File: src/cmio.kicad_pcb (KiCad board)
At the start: 2 copper layers, 72.4 x 36.8 mm, 37 parts, among them J15 CONN_01X02, J2 BANK0, J4 DSI0, J5 CM3Lite, J6 DSI1, J8 BANK1, J9 Micro_SD_Card_TFP09_2_12B, U1 ISL91107IR, U2 LD3985M18R, U3 LD3985M28R

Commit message: Some changes to old design
Signed-off-by: Mahyar Koshkouei <mk@deltabeard.com>
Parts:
- removed 1V8: TEST_1V8, Measurement_Points:Measurement_Point_Round-SMD-Pad_Small
- removed 2V8: TEST_2V8, Measurement_Points:Measurement_Point_Round-SMD-Pad_Small
- removed 3V3: TEST_3V3, Measurement_Points:Measurement_Point_Round-SMD-Pad_Small
- removed 5V: TEST_5V, Measurement_Points:Measurement_Point_Round-SMD-Pad_Small
- removed GND: TEST_GND, Measurement_Points:Measurement_Point_Round-SMD-Pad_Small
- removed J15: CONN_01X02, Pin_Headers:Pin_Header_Straight_2x01_Pitch2.54mm_SMD
- removed J2: BANK0, Pin_Headers:Pin_Header_Straight_2x20_Pitch2.54mm_SMD
- removed J6: DSI1, Pin_Headers:Pin_Header_Straight_2x05_Pitch2.54mm_SMD
- removed JP4: 3.3 OUT, Pin_Headers:Pin_Header_Straight_2x01_Pitch2.54mm_SMD
- removed JP6: PWRUSB, Pin_Headers:Pin_Header_Straight_2x01_Pitch2.54mm_SMD
- removed JP7: Disable SD Card, Pin_Headers:Pin_Header_Straight_2x01_Pitch2.54mm_SMD
- removed POWER: USB_POWER, foot:Micro_USB_B_10104110_no_holes
- removed RESET: Reset, Buttons_Switches_SMD:SW_SPST_TL3342
- removed TV: TVOUT, foot:RCA_PHONO
- removed USB: USB_OTG, foot:Micro_USB_B_10104110_no_holes
- added C11: 4.7uF, Capacitors_SMD:C_1206_HandSoldering, F.Cu at (208.2, 67.3)
- added J1: USB_POWER, foot:Micro_USB_B_10104110, F.Cu at (178.4, 61.0)
- added J10: CM3Lite, foot:Socket_SODIMM_DDR1-2_TE_1612618, B.Cu at (190.5, 76.2)
- added J11: TVOUT, foot:RCA_PHONO, F.Cu at (157.5, 83.8)
- added J12: BANK1, Pin_Headers:Pin_Header_Straight_2x10_Pitch2.54mm_SMD, F.Cu at (196.8, 73.7)
- added J13: Micro_SD_Card_TFP09_2_12B, foot:TFP09-2-12B, F.Cu at (213.4, 66.0)
- added J7: TEST_GND, Measurement_Points:Measurement_Point_Round-SMD-Pad_Small, F.Cu at (157.5, 58.4)
- added JP1: 3.3 OUT, Pin_Headers:Pin_Header_Straight_2x01_Pitch2.54mm_SMD, F.Cu at (204.5, 62.9)
- added JP2: PWRUSB, Pin_Headers:Pin_Header_Straight_2x01_Pitch2.54mm_SMD, F.Cu at (177.0, 64.3)
- added SW1: Reset, Buttons_Switches_SMD:SW_SPST_TL3342, F.Cu at (168.9, 82.5)
- C10: value 4.7uF -> 22uF; moved to F.Cu
- C2, C4, C8, R1, R2: moved to B.Cu
- C3: value 22uF -> 10nF
- C5: value 10nF -> 1uF
- C6: value 22uF -> 1uF
- C7: value 1uF -> 22uF
- J4: value DSI0 -> TEST_3V3; footprint Pin_Headers:Pin_Header_Straight_2x03_Pitch2.54mm_SMD -> Measurement_Points:Measurement_Point_Round-SMD-Pad_Small
- J5: value CM3Lite -> TEST_2V8; footprint foot:Socket_SODIMM_DDR1-2_TE_1612618 -> Measurement_Points:Measurement_Point_Round-SMD-Pad_Small; moved to F.Cu
- J8: value BANK1 -> BANK0; footprint Pin_Headers:Pin_Header_Straight_2x10_Pitch2.54mm_SMD -> Pin_Headers:Pin_Header_Straight_2x20_Pitch2.54mm_SMD
- J9: value Micro_SD_Card_TFP09_2_12B -> USB_OTG; footprint foot:TFP09-2-12B -> foot:Micro_USB_B_10104110; moved to F.Cu
- U1: value ISL91107IR -> LD3985M18R; footprint foot:20_TQFP -> TO_SOT_Packages_SMD:SOT-23-5
- U2: value LD3985M18R -> LD3985M28R; moved to B.Cu
- U3: value LD3985M28R -> ISL91107IR; footprint TO_SOT_Packages_SMD:SOT-23-5 -> foot:20_TQFP
- moved C9 107.4 mm to (195.6, 64.8), turned to 90 degrees
- moved L1 101.2 mm to (190.5, 58.4)
- moved C7 94.1 mm to (182.9, 64.8), turned to 270 degrees
- moved U3 86.6 mm to (190.5, 64.1), turned to 270 degrees
- moved C5 82.6 mm to (185.4, 64.8), turned to 270 degrees
- moved C6 82.2 mm to (169.5, 75.6)
- moved U1 82.0 mm to (169.5, 72.4), turned to 180 degrees
- moved C3 80.7 mm to (163.8, 71.1), turned to 180 degrees
- moved C1 78.8 mm to (175.3, 71.1), turned to 0 degrees
- moved C4 78.7 mm to (172.7, 67.3)
- moved U2 74.4 mm to (167.0, 66.7), turned to 270 degrees
- moved J8 74.2 mm to (199.4, 82.5)
- moved R1 69.4 mm to (214.0, 66.7), turned to 90 degrees
- moved J4 69.0 mm to (157.5, 61.0), turned to 0 degrees
- moved C10 68.6 mm to (198.1, 64.8), turned to 90 degrees
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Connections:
- C1 pad 1: +5V -> +3V3
- C10 pad 1: +3V3 -> GND
- C10 pad 2: GND -> Net-(C10-Pad2)
- C2 pad 1: +5V -> +3V3
- C3 pad 1: +5V -> Net-(C3-Pad1)
- C5 pad 1: Net-(C5-Pad1) -> +5V
- C6 pad 1: GND -> +1V8
- C6 pad 2: Net-(C6-Pad2) -> GND
- C7 pad 1: +1V8 -> +5V
- C9 pad 2: Net-(C6-Pad2) -> Net-(C10-Pad2)
- J4 pad 1: /DSI0_0 -> +3V3
- J5 pad 1: GND -> +2V8
- J8 pad 10: /BCM_40 -> /BCM_15
- J8 pad 11: /BCM_32 -> /BCM_17
- J8 pad 12: /BCM_41 -> /BCM_18
- J8 pad 13: /BCM_33 -> /BCM_27
- J8 pad 14: /BCM_42 -> GND
- J8 pad 15: /BCM_34 -> /BCM_22
- J8 pad 16: /BCM_43 -> /BCM_23
- J8 pad 17: /BCM_35 -> +3V3
- J8 pad 18: /BCM_44 -> /BCM_24
- J8 pad 19: /BCM_36 -> /BCM_10
- J8 pad 2: GND -> +5V
- J8 pad 20: /BCM_45 -> GND
- J8 pad 3: /BCM_28 -> /BCM_2
- J8 pad 4: /BCM_37 -> +5V
- J8 pad 5: /BCM_29 -> /BCM_3
- J8 pad 6: /BCM_38 -> GND
- J8 pad 7: /BCM_30 -> /BCM_4
- J8 pad 8: /BCM_39 -> /BCM_14
- J8 pad 9: /BCM_31 -> GND
- J9 pad 1: DAT2 -> Net-(J9-Pad1)
- J9 pad 2: DAT3 -> /D-
- J9 pad 3: CMD -> /D+
- J9 pad 4: +3V3 -> OTDIG
- J9 pad 5: CLK -> GND
- U1 pad 1: Net-(L1-Pad1) -> +3V3
- U1 pad 2: Net-(L1-Pad1) -> GND
- U1 pad 3: GND -> +3V3
- U1 pad 4: GND -> Net-(C3-Pad1)
- U1 pad 5: Net-(L1-Pad2) -> +1V8
- U2 pad 1: +5V -> +3V3
- U2 pad 3: +5V -> +3V3
- U2 pad 5: +1V8 -> +2V8
- U3 pad 1: +5V -> Net-(L1-Pad1)
- U3 pad 2: GND -> Net-(L1-Pad1)
- U3 pad 3: +5V -> GND
- U3 pad 4: Net-(C5-Pad1) -> GND
- U3 pad 5: +2V8 -> Net-(L1-Pad2)
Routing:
- net +3V3: track 208.1 -> 105.8 mm, vias 14 -> 8
- net +5V: track 132.1 -> 31.1 mm, vias 5 -> 2
- net Net-(J5-Pad177): track 39.6 -> 0.00 mm, vias 1 -> 0
- net +2V8: track 58.9 -> 20.1 mm, vias 2 -> 1
- net /DSI0_1: track 29.1 -> 0.00 mm, vias 1 -> 0
- net /DSI0_0: track 27.4 -> 0.00 mm, vias 1 -> 0
- net +1V8: track 49.6 -> 22.2 mm
- net /BCM_44: track 43.5 -> 16.2 mm
- net /DSI0_3: track 26.7 -> 0.00 mm, vias 1 -> 0
- net /DSI1_8: track 24.7 -> 0.00 mm, vias 1 -> 0
- net TVDAC: track 23.8 -> 0.00 mm, vias 3 -> 0
- net /DSI0_2: track 23.4 -> 0.00 mm, vias 1 -> 0
- net /DSI1_6: track 21.8 -> 0.00 mm, vias 1 -> 0
- net /BCM_45: track 36.4 -> 14.9 mm
- net /DSI1_9: track 21.3 -> 0.00 mm, vias 1 -> 0
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- added copper zone on F.Cu, net +3V3
- added copper zone on F.Cu, net Net-(C10-Pad2)
- added copper zone on F.Cu, net Net-(L1-Pad1)
- added copper zone on F.Cu, net Net-(L1-Pad2)
- removed copper zone on F.Cu, net Net-(C6-Pad2)
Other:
- board size 72.4 x 36.8 mm -> 71.1 x 31.7 mm
- net class Default: clearance 0.16 -> 0; trace_width 0.18 -> 0.25
- net class PWR: clearance 0.2 -> 0.25; trace_width 0.25 -> 0.35
- rule trace_clearance: 0.16 -> 0
- rule trace_min: 0.15 -> 0.2
- rule via_min_size: 0.5 -> 0.6
- board text removed: "GPL 3 Mahyar Koshkouei Custom CMIO Board"

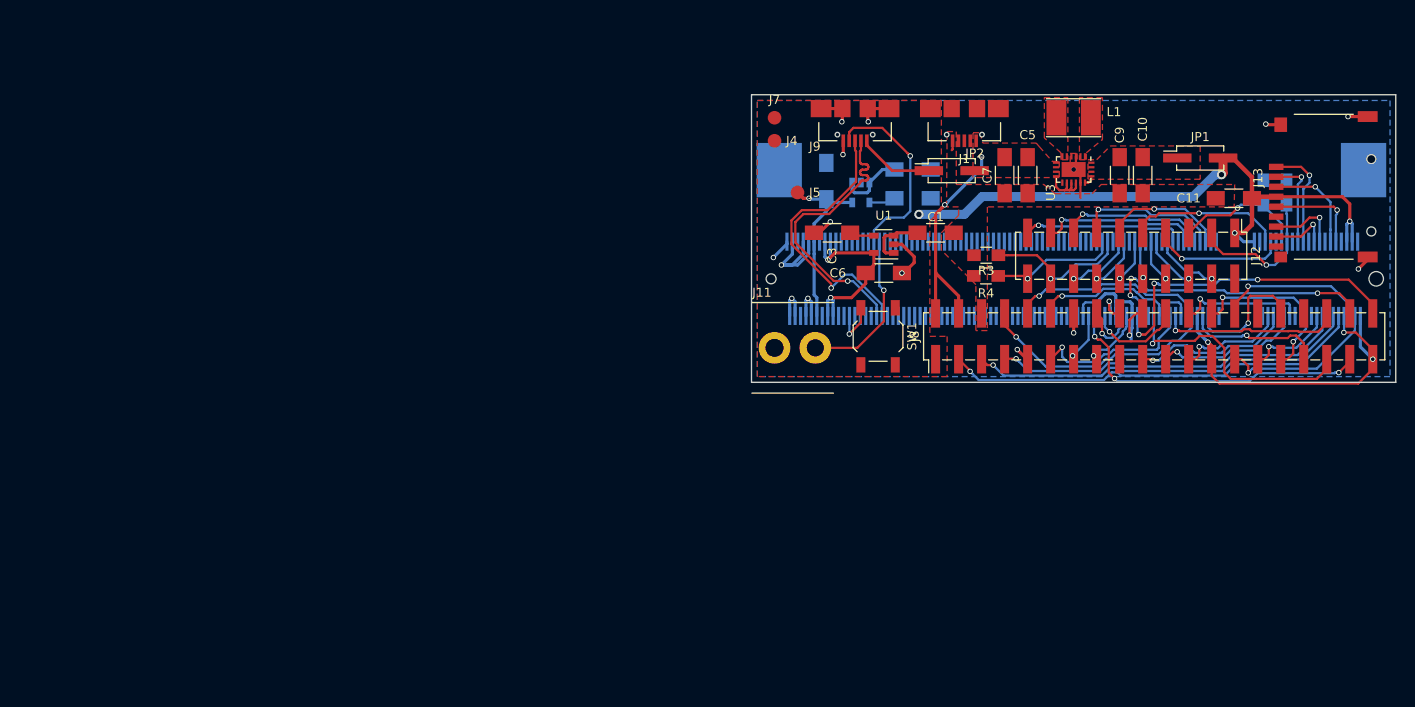
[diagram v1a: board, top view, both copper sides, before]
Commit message: Finish PCB Routing
Signed-off-by: Mahyar Koshkouei <mk@deltabeard.com>
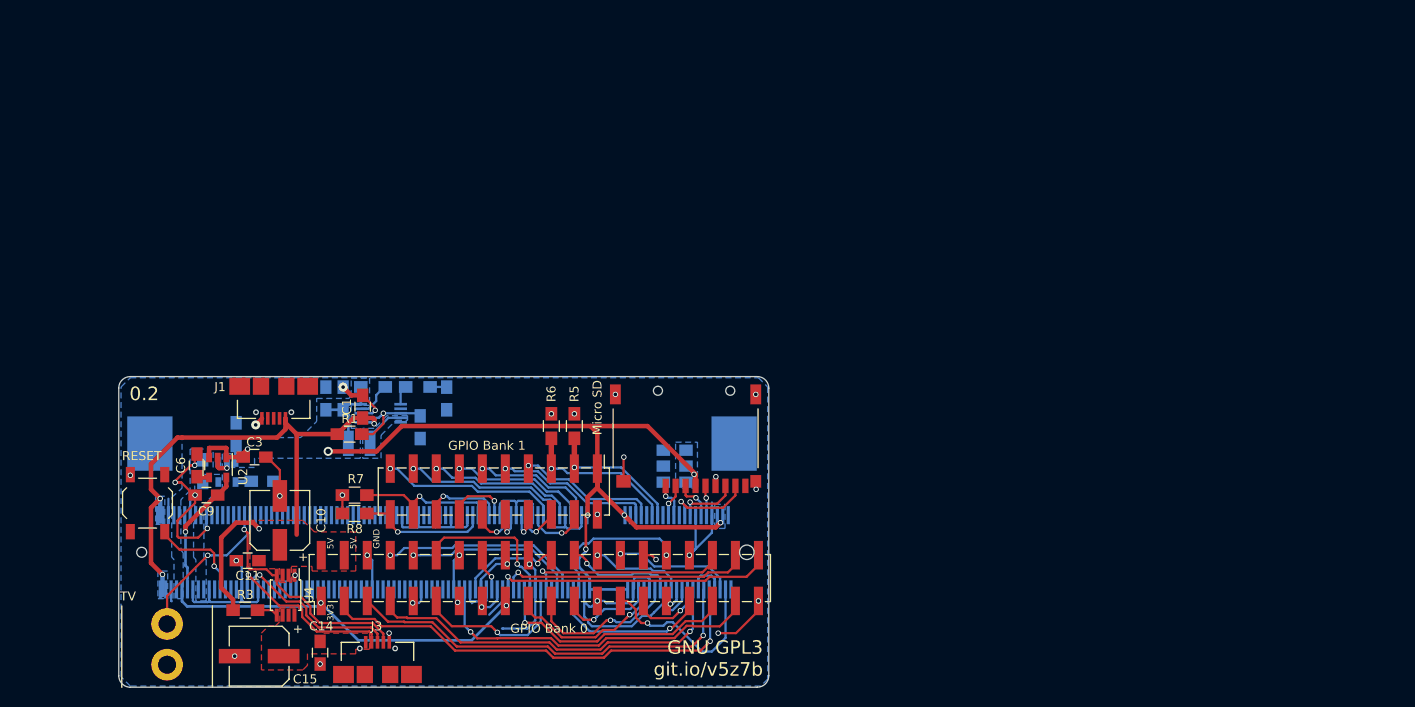
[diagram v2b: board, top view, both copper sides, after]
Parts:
- removed J10: CM3Lite, foot:Socket_SODIMM_DDR1-2_TE_1612618
- removed J11: TVOUT, foot:RCA_PHONO
- removed J12: BANK1, Pin_Headers:Pin_Header_Straight_2x10_Pitch2.54mm_SMD
- removed J13: Micro_SD_Card_TFP09_2_12B, foot:TFP09-2-12B
- removed J8: BANK0, Pin_Headers:Pin_Header_Straight_2x20_Pitch2.54mm_SMD
- removed J9: USB_OTG, foot:Micro_USB_B_10104110
- removed JP1: 3.3 OUT, Pin_Headers:Pin_Header_Straight_2x01_Pitch2.54mm_SMD
- removed JP2: PWRUSB, Pin_Headers:Pin_Header_Straight_2x01_Pitch2.54mm_SMD
- added C12: 10uF, Capacitors_SMD:C_0805_HandSoldering, B.Cu at (109.9, 89.4)
- added C13: 100pF, Capacitors_SMD:C_0805_HandSoldering, B.Cu at (108.0, 89.4)
- added C14: 0.1uF, Capacitors_SMD:C_0805_HandSoldering, F.Cu at (107.3, 117.5)
- added C15: 120uF, Capacitors_SMD:CP_Elec_6.3x5.8, F.Cu at (100.6, 117.9)
- added C16: 100pF, Capacitors_SMD:C_0805_HandSoldering, B.Cu at (146.5, 98.7)
- added C17: 0.1uF, Capacitors_SMD:C_0805_HandSoldering, B.Cu at (146.5, 96.9)
- added C18: 10uF, Capacitors_SMD:C_0805_HandSoldering, B.Cu at (146.5, 95.1)
- added J2: BANK0, Pin_Headers:Pin_Header_Straight_2x20_Pitch2.54mm_SMD, F.Cu at (131.6, 109.2)
- added J3: USB_OTG, foot:Micro_USB_B_10104110, F.Cu at (113.7, 116.3)
- added J6: BANK1, Pin_Headers:Pin_Header_Straight_2x10_Pitch2.54mm_SMD, F.Cu at (126.5, 99.7)
- added R5: 100K, Resistors_SMD:R_0805_HandSoldering, F.Cu at (135.4, 92.5)
- added R6: 100K, Resistors_SMD:R_0805_HandSoldering, F.Cu at (132.8, 92.5)
- added R7: 100K, Resistors_SMD:R_0805_HandSoldering, F.Cu at (111.1, 100.1)
- added R8: 100K, Resistors_SMD:R_0805_HandSoldering, F.Cu at (111.1, 102.1)
- added U4: AP2401, Housings_SSOP:MSOP-8_3x3mm_Pitch0.65mm, F.Cu at (103.5, 111.1)
- C1: value 1uF -> 10uF; footprint Capacitors_SMD:C_1206_HandSoldering -> Capacitors_SMD:C_0805_HandSoldering
- C10: value 22uF -> 120uF; footprint Capacitors_SMD:C_1206_HandSoldering -> Capacitors_SMD:CP_Elec_6.3x5.8
- C11: value 4.7uF -> 0.1uF; footprint Capacitors_SMD:C_1206_HandSoldering -> Capacitors_SMD:C_0805_HandSoldering
- C2, C8: footprint Capacitors_SMD:C_1206_HandSoldering -> Capacitors_SMD:C_0805_HandSoldering
- C3, C4: value 10nF -> 1uF; footprint Capacitors_SMD:C_1206_HandSoldering -> Capacitors_SMD:C_0805_HandSoldering
- C5: value 1uF -> 10nF; footprint Capacitors_SMD:C_1206_HandSoldering -> Capacitors_SMD:C_0805_HandSoldering; moved to B.Cu
- C6: value 1uF -> 10nF; footprint Capacitors_SMD:C_1206_HandSoldering -> Capacitors_SMD:C_0805_HandSoldering
- C7: value 22uF -> 100pF; footprint Capacitors_SMD:C_1206_HandSoldering -> Capacitors_SMD:C_0805_HandSoldering; moved to B.Cu
- C9: value 22uF -> 1uF; footprint Capacitors_SMD:C_1206_HandSoldering -> Capacitors_SMD:C_0805_HandSoldering
- J4: value TEST_3V3 -> CM3Lite; footprint Measurement_Points:Measurement_Point_Round-SMD-Pad_Small -> foot:Socket_SODIMM_DDR1-2_TE_1612618; moved to B.Cu
- J5: value TEST_2V8 -> TVOUT; footprint Measurement_Points:Measurement_Point_Round-SMD-Pad_Small -> foot:RCA_PHONO
- J7: value TEST_GND -> Micro_SD_Card_TFP09_2_12B; footprint Measurement_Points:Measurement_Point_Round-SMD-Pad_Small -> foot:TFP09-2-12B
- L1: value 1uH -> 3.3uH; footprint Inductors:Inductor_Taiyo-Yuden_NR-40xx_HandSoldering -> foot:Inductor_1008; moved to B.Cu
- R1: value 100K -> 100; moved to F.Cu
- R2: value 100K -> 82K
- R3: value 100K -> 10K
- R4: value 100K -> 680K; moved to B.Cu
- U1: moved to B.Cu
- U2: moved to F.Cu
- U3: value ISL91107IR -> AP6015; footprint foot:20_TQFP -> Housings_SSOP:MSOP-10_3x3mm_Pitch0.5mm; moved to B.Cu
- moved C11 116.0 mm to (99.3, 107.3)
- moved C9 106.8 mm to (94.8, 100.1), turned to 180 degrees
- moved R1 106.8 mm to (110.6, 93.3), turned to 0 degrees
- moved C10 102.6 mm to (102.9, 102.9)
- moved R2 95.8 mm to (118.1, 88.1), turned to 180 degrees
- moved C5 91.0 mm to (101.0, 98.6), turned to 0 degrees
- moved R3 90.7 mm to (99.1, 112.8), turned to 0 degrees
- moved J5 87.0 mm to (90.4, 118.8), turned to 90 degrees
- moved L1 86.7 mm to (111.6, 94.4)
- moved SW1 82.7 mm to (88.3, 101.0), turned to 90 degrees
- moved J1 82.2 mm to (102.2, 91.6)
- moved U3 81.1 mm to (114.0, 91.0), turned to 0 degrees
- moved C2 80.2 mm to (98.0, 93.3), turned to 90 degrees
- moved C6 78.7 mm to (93.7, 96.8), turned to 90 degrees
- moved U2 77.2 mm to (96.0, 97.0)
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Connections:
- C1 pad 1: +3V3 -> +5V
- C10 pad 1: GND -> +5V
- C10 pad 2: Net-(C10-Pad2) -> GND
- C11 pad 1: +3V3 -> +5V
- C3 pad 1: Net-(C3-Pad1) -> +3V3
- C5 pad 1: +5V -> Net-(C5-Pad1)
- C6 pad 1: +1V8 -> Net-(C6-Pad1)
- C7 pad 1: +5V -> GND
- C7 pad 2: GND -> Net-(C7-Pad2)
- C8 pad 1: +2V8 -> +1V8
- C9 pad 1: GND -> +2V8
- C9 pad 2: Net-(C10-Pad2) -> GND
- J1 pad 6: GND -> Net-(J1-Pad6)
- J4 pad 1: +3V3 -> GND
- J5 pad 1: +2V8 -> Net-(J4-Pad166)
- J7 pad 1: GND -> DAT2
- L1 pad 2: Net-(L1-Pad2) -> +3V3
- R1 pad 1: /BCM_28 -> +5V
- R1 pad 2: GND -> Net-(C4-Pad1)
- R2 pad 1: /BCM_29 -> Net-(C7-Pad2)
- R2 pad 2: GND -> Net-(R2-Pad2)
- R3 pad 1: /BCM_44 -> +5V
- R3 pad 2: GND -> Net-(R3-Pad2)
- R4 pad 1: /BCM_45 -> Net-(R4-Pad1)
- R4 pad 2: GND -> +3V3
- SW1 pad 2: Net-(J10-Pad177) -> Net-(J4-Pad177)
- U1 pad 4: Net-(C3-Pad1) -> Net-(C5-Pad1)
- U2 pad 4: Net-(C4-Pad1) -> Net-(C6-Pad1)
- U3 pad 1: Net-(L1-Pad1) -> +5V
- U3 pad 10: +5V -> GND
- U3 pad 2: Net-(L1-Pad1) -> Net-(C4-Pad1)
- U3 pad 4: GND -> Net-(R4-Pad1)
- U3 pad 5: Net-(L1-Pad2) -> +3V3
- U3 pad 6: Net-(L1-Pad2) -> Net-(R2-Pad2)
- U3 pad 7: +5V -> (no net)
- U3 pad 8: +5V -> Net-(C4-Pad1)
- U3 pad 9: +5V -> Net-(L1-Pad1)
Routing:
- net GND: track 96.4 -> 183.8 mm, vias 14 -> 33
- net +5V: track 31.1 -> 74.5 mm, vias 2 -> 4
- net +3V3: track 105.8 -> 149.0 mm, vias 8 -> 9
- net OTGID: track 0.00 -> 25.9 mm, vias 0 -> 1
- net +1V8: track 22.2 -> 0.00 mm, vias 2 -> 0
- net OTDIG: track 21.4 -> 0.00 mm, vias 1 -> 0
- net Net-(J10-Pad166): track 17.8 -> 0.00 mm, vias 1 -> 0
- net Net-(J4-Pad166): track 0.00 -> 17.0 mm, vias 0 -> 1
- net /D+: track 31.6 -> 19.2 mm
- net /D-: track 31.6 -> 19.4 mm
- net Net-(J4-Pad177): track 0.00 -> 10.9 mm, vias 0 -> 1
- net Net-(J9-Pad1): track 8.50 -> 0.00 mm
- net Net-(C4-Pad1): track 2.96 -> 10.9 mm, vias 0 -> 1
- net DAT2: track 11.7 -> 3.90 mm
- net CLK: track 10.4 -> 3.28 mm
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- added copper zone on B.Cu, net +1V8
- added copper zone on B.Cu, net +3V3
- added copper zone on B.Cu, net +5V
- added copper zone on F.Cu, net Net-(C14-Pad1)
- added copper zone on B.Cu, net Net-(L1-Pad1)
- removed copper zone on F.Cu, net +3V3
- removed copper zone on F.Cu, net GND
- removed copper zone on F.Cu, net Net-(C10-Pad2)
- removed copper zone on F.Cu, net Net-(L1-Pad1)
- removed copper zone on F.Cu, net Net-(L1-Pad2)
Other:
- board size 71.1 x 31.7 mm -> 71.8 x 34.3 mm
- net class Default: clearance 0 -> 0.2
- net class PWR removed
- net class Power added: clearance 0.2, trace_width 0.3, via_dia 0.6, via_drill 0.4
- rule pad_to_mask_clearance: 0.2 -> 0
- rule trace_clearance: 0 -> 0.2
- rule via_min_size: 0.6 -> 0.4
- board text added: "0.2"
- board text added: "3V3"
- board text added: "5V"
- board text added: "GND"
- board text added: "GNU GPL3 git.io/v5z7b"
- board text added: "GPIO Bank 0"
- board text added: "GPIO Bank 1"
- board text added: "Micro SD"
- board text added: "RESET"
- board text added: "Raspberry Pi Compute Module"
- board text added: "TV"

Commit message: Improve CM3 Footprint
Additionally removed electrolytic capacitors.
Re-annotated components and cleared board.

Signed-off-by: Mahyar Koshkouei <mk@deltabeard.com>
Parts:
- removed C1, C12, C18: 10uF, Capacitors_SMD:C_0805_HandSoldering
- removed C10, C15: 120uF, Capacitors_SMD:CP_Elec_6.3x5.8
- removed C11, C14, C17: 0.1uF, Capacitors_SMD:C_0805_HandSoldering
- removed C13, C16, C7: 100pF, Capacitors_SMD:C_0805_HandSoldering
- removed C2, C3, C4, C8, C9: 1uF, Capacitors_SMD:C_0805_HandSoldering
- removed C5, C6: 10nF, Capacitors_SMD:C_0805_HandSoldering
- removed J1: USB_POWER, foot:Micro_USB_B_10104110
- removed J2: BANK0, Pin_Headers:Pin_Header_Straight_2x20_Pitch2.54mm_SMD
- removed J3: USB_OTG, foot:Micro_USB_B_10104110
- removed J4: CM3Lite, foot:Socket_SODIMM_DDR1-2_TE_1612618
- removed J5: TVOUT, foot:RCA_PHONO
- removed J6: BANK1, Pin_Headers:Pin_Header_Straight_2x10_Pitch2.54mm_SMD
- removed J7: Micro_SD_Card_TFP09_2_12B, foot:TFP09-2-12B
- removed L1: 3.3uH, foot:Inductor_1008
- removed R1: 100, Resistors_SMD:R_0805_HandSoldering
- removed R2: 82K, Resistors_SMD:R_0805_HandSoldering
- removed R3: 10K, Resistors_SMD:R_0805_HandSoldering
- removed R4: 680K, Resistors_SMD:R_0805_HandSoldering
- removed R5, R6, R7, R8: 100K, Resistors_SMD:R_0805_HandSoldering
- removed SW1: Reset, Buttons_Switches_SMD:SW_SPST_TL3342
- removed U1: LD3985M18R, TO_SOT_Packages_SMD:SOT-23-5
- removed U2: LD3985M28R, TO_SOT_Packages_SMD:SOT-23-5
- removed U3: AP6015, Housings_SSOP:MSOP-10_3x3mm_Pitch0.5mm
- removed U4: AP2401, Housings_SSOP:MSOP-8_3x3mm_Pitch0.65mm
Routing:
- net GND: track 183.8 -> 0.00 mm, vias 33 -> 0
- net +3V3: track 149.0 -> 0.00 mm, vias 9 -> 0
- net +5V: track 74.5 -> 0.00 mm, vias 4 -> 0
- net /BCM_2: track 50.1 -> 0.00 mm, vias 1 -> 0
- net /BCM_3: track 45.4 -> 0.00 mm, vias 1 -> 0
- net /BCM_4: track 41.5 -> 0.00 mm, vias 1 -> 0
- net /BCM_26: track 37.5 -> 0.00 mm, vias 1 -> 0
- net /BCM_21: track 31.1 -> 0.00 mm, vias 1 -> 0
- net /BCM_20: track 27.9 -> 0.00 mm, vias 1 -> 0
- net /BCM_19: track 27.7 -> 0.00 mm, vias 1 -> 0
- net OTGID: track 25.9 -> 0.00 mm, vias 1 -> 0
- net /BCM_14: track 22.5 -> 0.00 mm, vias 1 -> 0
- net /BCM_16: track 22.3 -> 0.00 mm, vias 1 -> 0
- net /BCM_0: track 20.7 -> 0.00 mm, vias 1 -> 0
- net /BCM_36: track 19.7 -> 0.00 mm, vias 1 -> 0
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- removed copper zone on B.Cu, net +1V8
- removed copper zone on B.Cu, net +3V3
- removed copper zone on B.Cu, net +5V
- removed copper zone on F.Cu, net +5V
- removed copper zone on B.Cu, net GND
- removed copper zone on F.Cu, net Net-(C14-Pad1)
- removed copper zone on B.Cu, net Net-(L1-Pad1)
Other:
- board outline removed
- board text removed: "0.2"
- board text removed: "3V3"
- board text removed: "5V"
- board text removed: "GND"
- board text removed: "GNU GPL3 git.io/v5z7b"
- board text removed: "GPIO Bank 0"
- board text removed: "GPIO Bank 1"
- board text removed: "Micro SD"
- board text removed: "RESET"
- board text removed: "Raspberry Pi Compute Module"
- board text removed: "TV"

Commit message: Replaced ICs
Using buck converters with simpler design requirements and lower cost.
Using an LDO for VDAC due to lower noise and low current requirements.

Signed-off-by: Mahyar Koshkouei <mahyar.koshkouei@gmail.com>
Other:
- net class Default: via_dia 0.6 -> 0.8
- net class Power: via_dia 0.6 -> 0.8
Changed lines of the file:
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@@
   (title_block
     (title "Compute Module IO Board")
-    (date 2017-09-04)
+    (date 2017-09-17)
     (company "Mahyar Koshkouei")
     (comment 1 "GPL 3")
@@
     (46 B.CrtYd user)
     (47 F.CrtYd user)
-    (48 B.Fab user hide)
-    (49 F.Fab user hide)
+    (48 B.Fab user)
+    (49 F.Fab user)
   )
   (setup
@@
     (segment_width 0.2)
     (edge_width 0.1)
-    (via_size 0.6)
+    (via_size 0.8)
     (via_drill 0.4)
     (via_min_size 0.4)
@@
     (pad_to_mask_clearance 0)
     (aux_axis_origin 0 0)
-    (visible_elements FFFFFF7F)
+    (visible_elements FFFFF77F)
     (pcbplotparams
       (layerselection 0x00010_fffffffe)
@@
     (clearance 0.2)
     (trace_width 0.25)
-    (via_dia 0.6)
+    (via_dia 0.8)
     (via_drill 0.4)
     (uvia_dia 0.3)
@@
     (clearance 0.2)
     (trace_width 0.3)
-    (via_dia 0.6)
+    (via_dia 0.8)
     (via_drill 0.4)
     (uvia_dia 0.3)
